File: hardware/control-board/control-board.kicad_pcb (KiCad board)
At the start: 2 copper layers, 39.5 x 106.5 mm, 28 parts, among them J1 JACK_2P, J12 JACK_2P, J14 Top Left(M), J16 Top Right (M), J18 Bottom Left(M), J2 JACK_2P, J20 Bottom Right(M), J3 JACK_2P, J4 JACK_2P, J5 JACK_2P, J6 JACK_2P, J7 JACK_2P, J8 JACK_2P

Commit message: chore: restructure project
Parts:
- RV3, RV4, RV5: footprint cem-3340:Alpha Potentiometer -> Eurorack Common:Alpha Potentiometer
- S1: footprint cem-3340:Sub-Miniature SPDT -> Eurorack Common:Sub-Miniature SPDT
- moved C6 0.11 mm to (28.6, 90.4)
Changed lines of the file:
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@@
 		)
 		(embedded_fonts no)
-		(model "${KIPRJMOD}/../libs/3D/Thonkicon.step"
+		(model "${KIPRJMOD}/../shared/3dmodels/Thonkicon.step"
 			(offset
 				(xyz 0 -7 0)
@@
 		)
 		(embedded_fonts no)
-		(model "${KIPRJMOD}/../libs/3D/Thonkicon.step"
+		(model "${KIPRJMOD}/../shared/3dmodels/Thonkicon.step"
 			(offset
 				(xyz 0 -7 0)
@@
 		)
 	)
-	(footprint "cem-3340:Sub-Miniature SPDT"
+	(footprint "Eurorack Common:Sub-Miniature SPDT"
 		(layer "F.Cu")
 		(at 29.9 84.616 90)
@@
 			)
 		)
-		(property "Datasheet" "~"
+		(property "Datasheet" ""
 			(at 0 0 90)
 			(layer "F.Fab")
@@
 			)
 		)
-		(property "Description" "Switch, single pole double throw"
+		(property "Description" ""
 			(at 0 0 90)
 			(layer "F.Fab")
@@
 		)
 		(embedded_fonts no)
-		(model "${KIPRJMOD}/../libs/3D/200-MSP-1-T3-B1-M2-PE-rev2.step"
+		(model "${KIPRJMOD}/../shared/3dmodels/Subminiture-SPDT.step"
 			(offset
 				(xyz 0 0 0)
@@
 		)
 	)
-	(footprint "cem-3340:Alpha Potentiometer"
+	(footprint "Eurorack Common:Alpha Potentiometer"
 		(layer "F.Cu")
 		(at 22.315 71.871)
@@
 			)
 		)
-		(property "Datasheet" "~"
+		(property "Datasheet" ""
 			(at 0 0 0)
 			(layer "F.Fab")
@@
 			)
 		)
-		(property "Description" "Potentiometer"
+		(property "Description" ""
 			(at 0 0 0)
 			(layer "F.Fab")
@@
 		)
 		(embedded_fonts no)
-		(model "${KIPRJMOD}/../libs/3D/ALPHA-RD901F-40.step"
+		(model "${KIPRJMOD}/../shared/3dmodels/Alpha-Pot.step"
 			(offset
-				(xyz 2.5 7 7)
+				(xyz 2.5 7.5 7)
 			)
 			(scale
@@
 		)
 		(embedded_fonts no)
-		(model "${KIPRJMOD}/../libs/3D/Thonkicon.step"
+		(model "${KIPRJMOD}/../shared/3dmodels/Thonkicon.step"
 			(offset
 				(xyz 0 -7 0)
@@
 		)
 		(embedded_fonts no)
-		(model "${KIPRJMOD}/../libs/3D/Thonkicon.step"
+		(model "${KIPRJMOD}/../shared/3dmodels/Thonkicon.step"
 			(offset
 				(xyz 0 -7 0)
@@
 		)
 	)
-	(footprint "cem-3340:Alpha Potentiometer"
+	(footprint "Eurorack Common:Alpha Potentiometer"
 		(layer "F.Cu")
 		(at 32.465 40.896)
@@
 			)
 		)
-		(property "Datasheet" "~"
+		(property "Datasheet" ""
 			(at 0 0 0)
 			(layer "F.Fab")
@@
 			)
 		)
-		(property "Description" "Potentiometer"
+		(property "Description" ""
 			(at 0 0 0)
 			(layer "F.Fab")
@@
 		)
 		(embedded_fonts no)
-		(model "${KIPRJMOD}/../libs/3D/ALPHA-RD901F-40.step"
+		(model "${KIPRJMOD}/../shared/3dmodels/Alpha-Pot.step"
 			(offset
-				(xyz 2.5 7 7)
+				(xyz 2.5 7.5 7)
 			)
 			(scale
@@
 		)
 	)
-	(footprint "cem-3340:Alpha Potentiometer"
+	(footprint "Eurorack Common:Alpha Potentiometer"
 		(layer "F.Cu")
 		(at 42.64 87.146)
@@
 			)
 		)
-		(property "Datasheet" "~"
+		(property "Datasheet" ""
 			(at 0 0 0)
 			(layer "F.Fab")
@@
 			)
 		)
-		(property "Description" "Potentiometer"
+		(property "Description" ""
 			(at 0 0 0)
 			(layer "F.Fab")
@@
 		)
 		(embedded_fonts no)
-		(model "${KIPRJMOD}/../libs/3D/ALPHA-RD901F-40.step"
+		(model "${KIPRJMOD}/../shared/3dmodels/Alpha-Pot.step"
 			(offset
-				(xyz 2.5 7.5 7.5)
+				(xyz 2.5 7.5 7)
 			)
 			(scale
@@
 		)
 		(embedded_fonts no)
-		(model "${KIPRJMOD}/../libs/3D/Thonkicon.step"
+		(model "${KIPRJMOD}/../shared/3dmodels/Thonkicon.step"
 			(offset
 				(xyz 0 -7 0)
@@
 		)
 		(embedded_fonts no)
-		(model "${KIPRJMOD}/../libs/3D/Thonkicon.step"
+		(model "${KIPRJMOD}/../shared/3dmodels/Thonkicon.step"
 			(offset
 				(xyz 0 -7 0)
@@
 		)
 		(embedded_fonts no)
-		(model "${KIPRJMOD}/../libs/3D/Thonkicon.step"
+		(model "${KIPRJMOD}/../shared/3dmodels/Thonkicon.step"
 			(offset
 				(xyz 0 -7 0)
@@
 	(footprint "Capacitor_THT:C_Rect_L4.6mm_W3.0mm_P2.50mm_MKS02_FKP02"
 		(layer "F.Cu")
-		(at 28.59 90.324)
+		(at 28.580556 90.434755)
 		(descr "C, Rect series, Radial, pin pitch=2.50mm, length*width=4.6*3.0mm^2, Capacitor, http://www.wima.de/DE/WIMA_MKS_02.pdf")
 		(tags "C Rect series Radial pin pitch 2.50mm length 4.6mm width 3.0mm Capacitor")
@@
 		)
 		(embedded_fonts no)
-		(model "${KIPRJMOD}/../libs/3D/Thonkicon.step"
+		(model "${KIPRJMOD}/../shared/3dmodels/Thonkicon.step"
 			(offset
 				(xyz 0 -7 0)
@@
 		)
 		(embedded_fonts no)
-		(model "${KIPRJMOD}/../libs/3D/Thonkicon.step"
+		(model "${KIPRJMOD}/../shared/3dmodels/Thonkicon.step"
 			(offset
 				(xyz 0 -7 0)
@@
 	)
 	(segment
-		(start 29.90993 84.616)
-		(end 31.84952 86.55559)
+		(start 31.84952 86.55559)
+		(end 31.84952 89.665791)
 		(width 0.5)
 		(layer "B.Cu")
@@
 	)
 	(segment
-		(start 31.84952 86.55559)
-		(end 31.84952 89.48648)
+		(start 29.90993 84.616)
+		(end 31.84952 86.55559)
 		(width 0.5)
 		(layer "B.Cu")
@@
 	)
 	(segment
-		(start 31.84952 89.48648)
-		(end 31.09 90.246)
+		(start 29.9 84.616)
+		(end 29.90993 84.616)
 		(width 0.5)
 		(layer "B.Cu")
@@
 	)
 	(segment
-		(start 29.9 84.616)
-		(end 29.90993 84.616)
+		(start 31.84952 89.665791)
+		(end 31.080556 90.434755)
 		(width 0.5)
 		(layer "B.Cu")
@@
 	)
 	(segment
-		(start 27.88 89.536)
-		(end 28.59 90.246)
+		(start 27.681801 89.536)
+		(end 28.580556 90.434755)
 		(width 0.5)
 		(layer "B.Cu")
@@
 	(segment
 		(start 19.74 89.536)
-		(end 27.88 89.536)
+		(end 27.681801 89.536)
 		(width 0.5)
 		(layer "B.Cu")

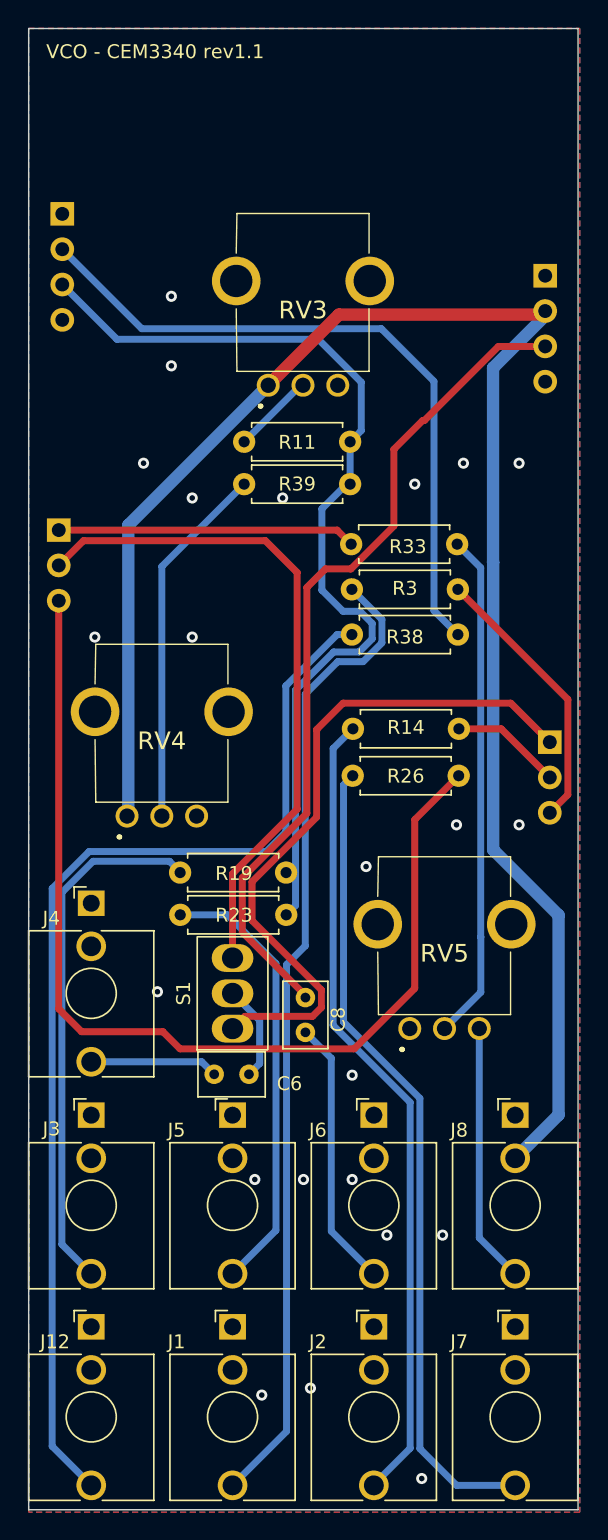
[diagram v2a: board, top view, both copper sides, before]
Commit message: feature: improve docs + front panel design
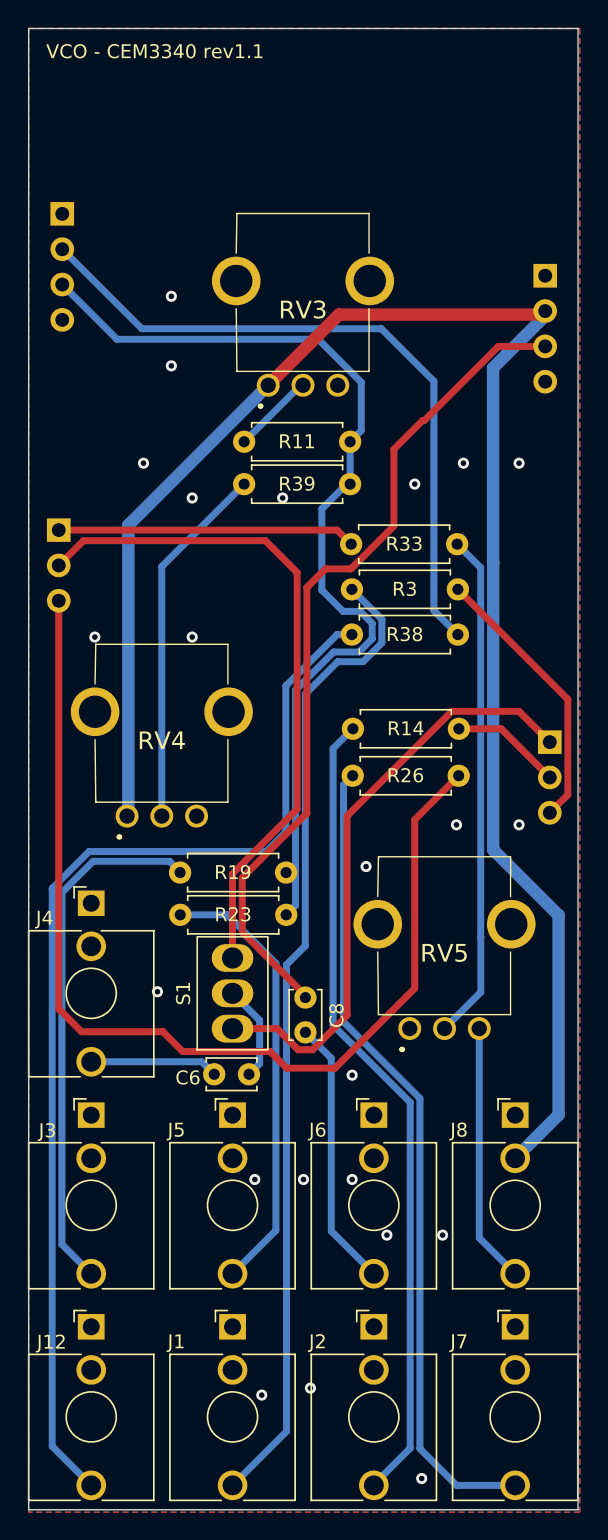
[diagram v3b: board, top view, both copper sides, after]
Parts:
- C6, C8: footprint Capacitor_THT:C_Rect_L4.6mm_W3.0mm_P2.50mm_MKS02_FKP02 -> Eurorack Common:C_Disc_D3.4mm_W2.1mm_P2.50mm
- J1, J12, J2, J3, J4, J5, J6, J7, J8: value JACK_2P -> ~; footprint Connector_Audio:Jack_3.5mm_QingPu_WQP-PJ398SM_Vertical_CircularHoles -> Eurorack Common:Thonkicon
- J14: value Top Left(M) -> ~; footprint Connector_PinHeader_2.54mm:PinHeader_1x04_P2.54mm_Vertical -> Eurorack Common:PinHeader_1x04_P2.54mm_Vertical
- J16: value Top Right (M) -> ~; footprint Connector_PinHeader_2.54mm:PinHeader_1x04_P2.54mm_Vertical -> Eurorack Common:PinHeader_1x04_P2.54mm_Vertical
- J18: value Bottom Left(M) -> ~; footprint Connector_PinHeader_2.54mm:PinHeader_1x03_P2.54mm_Vertical -> Eurorack Common:PinHeader_1x03_P2.54mm_Vertical
- J20: value Bottom Right(M) -> ~; footprint Connector_PinHeader_2.54mm:PinHeader_1x03_P2.54mm_Vertical -> Eurorack Common:PinHeader_1x03_P2.54mm_Vertical
- R11, R14, R19, R23, R26, R3, R33, R38, R39: footprint Resistor_THT:R_Axial_DIN0207_L6.3mm_D2.5mm_P7.62mm_Horizontal -> Eurorack Common:R_Axial_DIN0207_L6.3mm_D2.5mm_P7.62mm_Horizontal
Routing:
- net /SOFT_SYNC: track 49.7 -> 42.8 mm
- net /PULSE_RAW: track 74.5 -> 75.7 mm
